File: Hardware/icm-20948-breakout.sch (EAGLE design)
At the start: 11 parts, among them J1 455-1750-1-ND, J2 455-1750-1-ND, U1 NCP563, U2 NTS0104, U3 ICM-20948

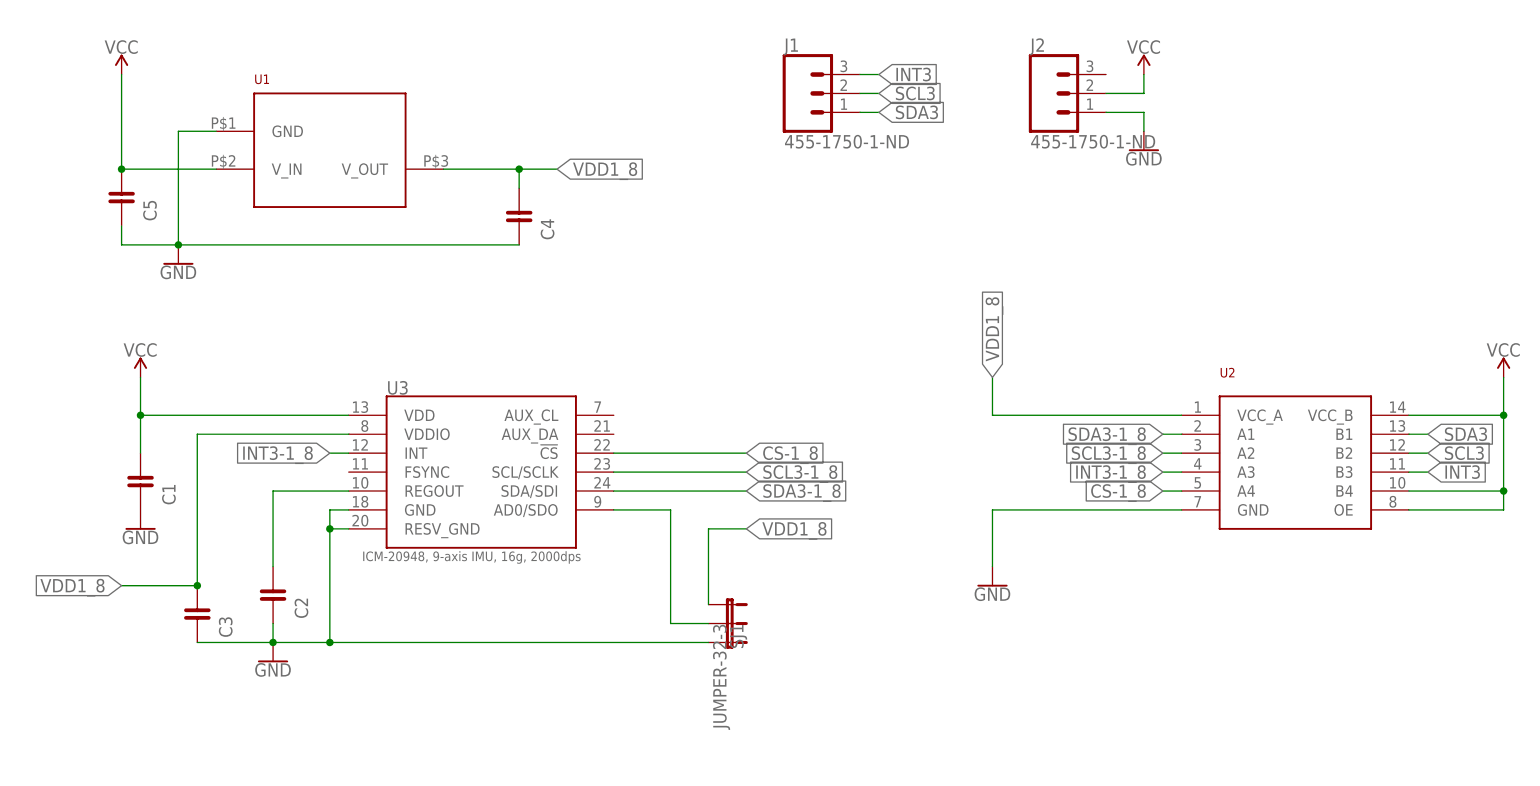
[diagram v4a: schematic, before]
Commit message: Went back to 0.6 inch width. Took away ground plane under icm. Added AD0 as an output pin with pull-up and therefore removed solder jumper.
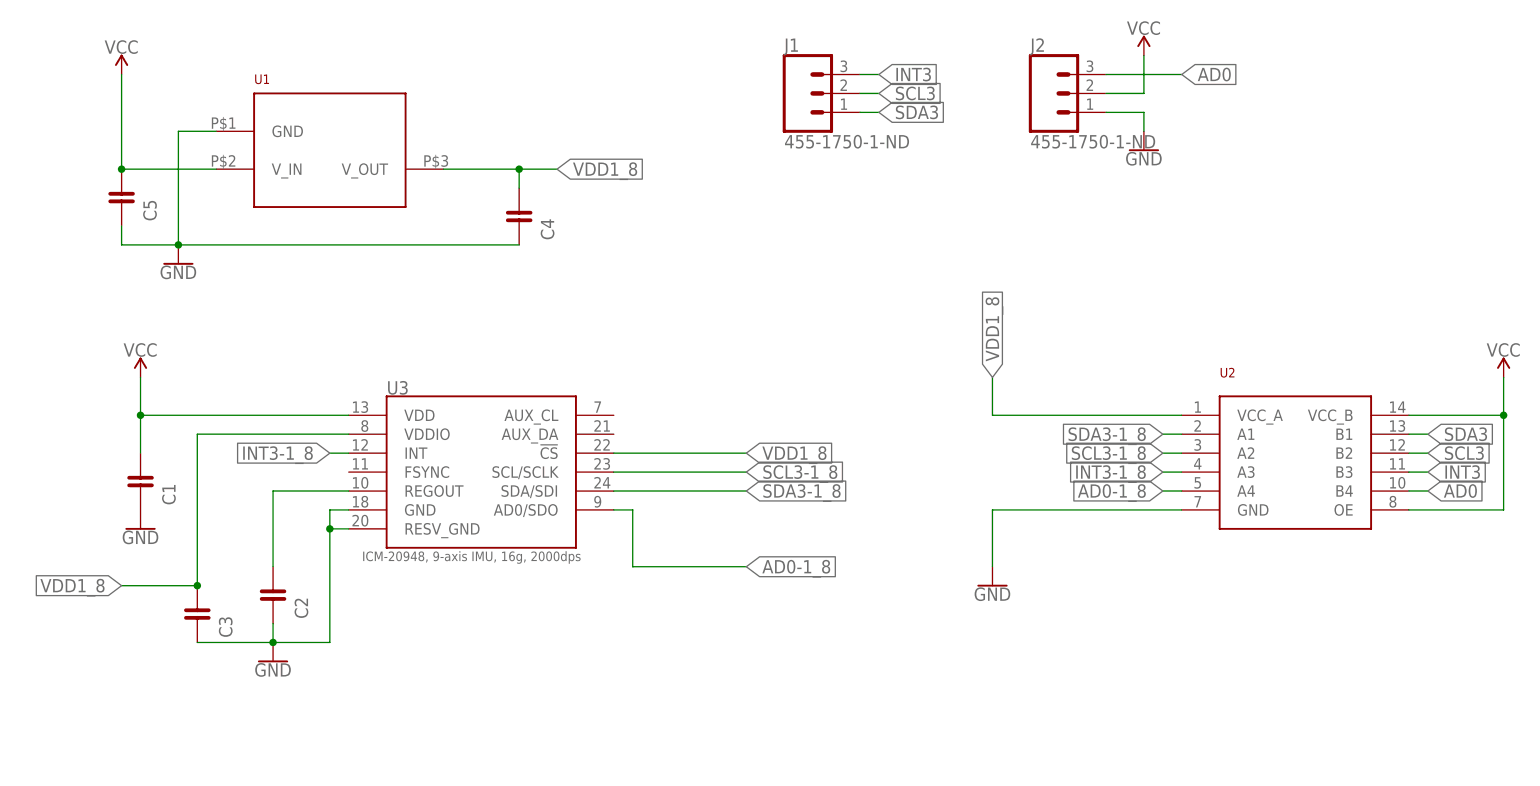
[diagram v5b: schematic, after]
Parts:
- removed SJ1: JUMPER-32-3, SparkFun-Passives:JUMPER-32-3
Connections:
- removed net CS-1_8: U2.A4, U3.!CS
- removed net N$2: SJ1.2, U3.AD0/SDO
- new net AD0: J2.3, U2.B4
- new net AD0-1_8: U2.A4, U3.AD0/SDO
- net GND: no longer SJ1.3
- net VCC: no longer U2.B4
- net VDD1_8: now also U3.!CS; no longer SJ1.1
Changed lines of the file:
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@@
 <part name="J1" library="SparkFun-Connectors" deviceset="CONN_03" device="" value="455-1750-1-ND"/>
 <part name="J2" library="SparkFun-Connectors" deviceset="CONN_03" device="" value="455-1750-1-ND"/>
-<part name="SJ1" library="SparkFun-Passives" deviceset="JUMPER-3" device="2-3" value="JUMPER-32-3"/>
 </parts>
 <sheets>
@@
 <attribute name="VALUE" x="134.62" y="40.894" size="1.778" layer="96" align="bottom-center"/>
 </instance>
-<instance part="SUPPLY3" gate="G$1" x="86.36" y="78.74" smashed="yes">
-<attribute name="VALUE" x="86.36" y="81.534" size="1.778" layer="96" align="bottom-center"/>
+<instance part="SUPPLY3" gate="G$1" x="86.36" y="81.28" smashed="yes">
+<attribute name="VALUE" x="86.36" y="84.074" size="1.778" layer="96" align="bottom-center"/>
 </instance>
 <instance part="GND5" gate="1" x="86.36" y="68.58" smashed="yes">
@@
 <attribute name="VALUE" x="71.12" y="68.834" size="1.778" layer="96" font="vector"/>
 <attribute name="NAME" x="71.12" y="81.788" size="1.778" layer="95" font="vector"/>
-</instance>
-<instance part="SJ1" gate="G$1" x="30.48" y="7.62" smashed="yes" rot="R270">
-<attribute name="NAME" x="30.861" y="5.08" size="1.778" layer="95" rot="R270"/>
-<attribute name="VALUE" x="28.575" y="5.08" size="1.778" layer="96" rot="R270"/>
 </instance>
 </instances>
@@
 </segment>
 <segment>
-<pinref part="SJ1" gate="G$1" pin="1"/>
-<wire x1="27.94" y1="7.62" x2="27.94" y2="17.78" width="0.1524" layer="91"/>
-<wire x1="27.94" y1="17.78" x2="33.02" y2="17.78" width="0.1524" layer="91"/>
-<label x="33.02" y="17.78" size="1.778" layer="95" xref="yes"/>
+<pinref part="U3" gate="G$1" pin="!CS"/>
+<wire x1="15.24" y1="27.94" x2="33.02" y2="27.94" width="0.1524" layer="91"/>
+<label x="33.02" y="27.94" size="1.778" layer="95" xref="yes"/>
 </segment>
 </net>
@@
 <wire x1="-30.48" y1="5.08" x2="-30.48" y2="2.54" width="0.1524" layer="91"/>
 <junction x="-30.48" y="2.54"/>
-<wire x1="27.94" y1="2.54" x2="-22.86" y2="2.54" width="0.1524" layer="91"/>
 <pinref part="C3" gate="G$1" pin="2"/>
 <wire x1="-22.86" y1="2.54" x2="-30.48" y2="2.54" width="0.1524" layer="91"/>
 <wire x1="-40.64" y1="2.54" x2="-30.48" y2="2.54" width="0.1524" layer="91"/>
-<pinref part="SJ1" gate="G$1" pin="3"/>
 <pinref part="U3" gate="G$1" pin="GND"/>
 <wire x1="-20.32" y1="20.32" x2="-22.86" y2="20.32" width="0.1524" layer="91"/>
 <wire x1="-22.86" y1="20.32" x2="-22.86" y2="17.78" width="0.1524" layer="91"/>
-<junction x="-22.86" y="2.54"/>
 <pinref part="U3" gate="G$1" pin="RESV_GND"/>
 <wire x1="-22.86" y1="17.78" x2="-22.86" y2="2.54" width="0.1524" layer="91"/>
@@
 <pinref part="SUPPLY4" gate="G$1" pin="VCC"/>
 <wire x1="134.62" y1="33.02" x2="134.62" y2="38.1" width="0.1524" layer="91"/>
-<wire x1="134.62" y1="33.02" x2="134.62" y2="22.86" width="0.1524" layer="91"/>
+<wire x1="134.62" y1="33.02" x2="134.62" y2="20.32" width="0.1524" layer="91"/>
 <junction x="134.62" y="33.02"/>
 <pinref part="U2" gate="G$1" pin="OE"/>
-<wire x1="134.62" y1="22.86" x2="134.62" y2="20.32" width="0.1524" layer="91"/>
 <wire x1="121.92" y1="20.32" x2="134.62" y2="20.32" width="0.1524" layer="91"/>
-<pinref part="U2" gate="G$1" pin="B4"/>
-<wire x1="121.92" y1="22.86" x2="134.62" y2="22.86" width="0.1524" layer="91"/>
-<junction x="134.62" y="22.86"/>
 </segment>
 <segment>
@@
 <pinref part="SUPPLY3" gate="G$1" pin="VCC"/>
 <wire x1="81.28" y1="76.2" x2="86.36" y2="76.2" width="0.1524" layer="91"/>
-<wire x1="86.36" y1="76.2" x2="86.36" y2="78.74" width="0.1524" layer="91"/>
+<wire x1="86.36" y1="76.2" x2="86.36" y2="81.28" width="0.1524" layer="91"/>
 </segment>
 </net>
@@
 </segment>
 </net>
-<net name="CS-1_8" class="0">
-<segment>
-<pinref part="U3" gate="G$1" pin="!CS"/>
-<wire x1="15.24" y1="27.94" x2="33.02" y2="27.94" width="0.1524" layer="91"/>
-<label x="33.02" y="27.94" size="1.778" layer="95" xref="yes"/>
+<net name="AD0-1_8" class="0">
+<segment>
+<pinref part="U3" gate="G$1" pin="AD0/SDO"/>
+<wire x1="15.24" y1="20.32" x2="17.78" y2="20.32" width="0.1524" layer="91"/>
+<wire x1="17.78" y1="20.32" x2="17.78" y2="12.7" width="0.1524" layer="91"/>
+<wire x1="17.78" y1="12.7" x2="33.02" y2="12.7" width="0.1524" layer="91"/>
+<label x="33.02" y="12.7" size="1.778" layer="95" xref="yes"/>
 </segment>
 <segment>
@@
 </segment>
 </net>
-<net name="N$2" class="0">
-<segment>
-<pinref part="U3" gate="G$1" pin="AD0/SDO"/>
-<wire x1="15.24" y1="20.32" x2="22.86" y2="20.32" width="0.1524" layer="91"/>
-<wire x1="22.86" y1="20.32" x2="22.86" y2="5.08" width="0.1524" layer="91"/>
-<pinref part="SJ1" gate="G$1" pin="2"/>
-<wire x1="22.86" y1="5.08" x2="27.94" y2="5.08" width="0.1524" layer="91"/>
-</segment>
-</net>
+<net name="AD0" class="0">
+<segment>
+<pinref part="J2" gate="J$1" pin="3"/>
+<wire x1="81.28" y1="78.74" x2="91.44" y2="78.74" width="0.1524" layer="91"/>
+<label x="91.44" y="78.74" size="1.778" layer="95" xref="yes"/>
+</segment>
+<segment>
+<pinref part="U2" gate="G$1" pin="B4"/>
+<wire x1="121.92" y1="22.86" x2="124.46" y2="22.86" width="0.1524" layer="91"/>
+<label x="124.46" y="22.86" size="1.778" layer="95" xref="yes"/>
+</segment>
+</net>
